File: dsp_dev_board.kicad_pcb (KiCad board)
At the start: 4 copper layers, 100 x 100 mm, 85 parts, among them J1 aux_mcu_power, J10 DX07S016JA1R1500, J2 audio_in, J3 audio_out, J4 9v_jack, J5 input_jack, J6 output_jack, J7 digital, J8 analog, J9 debug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

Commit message: WIP: QFN all the things
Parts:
- added J11: Conn_02x11_Odd_Even, Connector_PinHeader_2.54mm:PinHeader_2x11_P2.54mm_Vertical, F.Cu at (211.1, 104.0)
- added R11: 10k, Resistor_SMD:R_0603_1608Metric, F.Cu at (232.3, 109.6)
- added R23: 0 DNP, Resistor_SMD:R_0603_1608Metric, F.Cu at (210.8, 138.4)
- added R24: 0 DNP, Resistor_SMD:R_0603_1608Metric, F.Cu at (210.8, 140.9)
- added R25: 0 DNP, Resistor_SMD:R_0603_1608Metric, F.Cu at (214.8, 138.4)
- added R26: 0 DNP, Resistor_SMD:R_0603_1608Metric, F.Cu at (214.8, 140.9)
- added S1: TS-1187A-B-A-B, TactileSwitch:SW_TS-1187A-B-A-B, F.Cu at (235.3, 105.0)
- U3: value ATSAME51J18A-A -> ATSAME51J20A-A
- U4: value WM8731SEDS -> WM8731CLSEFL; footprint Package_SO:SSOP-28_5.3x10.2mm_P0.65mm -> Package_DFN_QFN:QFN-28-1EP_5x5mm_P0.5mm_EP3.35x3.35mm
- moved U4 1.96 mm to (156.2, 85.8), turned to 0 degrees
- moved R19 0.48 mm to (156.2, 79.7)
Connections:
- U4 pad 1: 3.3V -> /MCU/I2S2_MCK
- U4 pad 10: Net-(U4-Pad10) -> /Codec/ADC
- U4 pad 11: GND -> /Codec/WCLK
- U4 pad 12: /Codec/audio_out -> 3.3V
- U4 pad 14: 3.3V -> Net-(U4-Pad14)
- U4 pad 16: Net-(U4-Pad16) -> /Codec/audio_out
- U4 pad 18: Net-(U4-Pad18) -> 3.3V
- U4 pad 19: Net-(U4-Pad19) -> GND
- U4 pad 20: /Codec/audio_in -> Net-(U4-Pad20)
- U4 pad 21: Net-(R19-Pad1) -> Net-(U4-Pad21)
- U4 pad 22: /Codec/~CSB -> Net-(U4-Pad22)
- U4 pad 23: /Codec/SDIN -> Net-(U4-Pad23)
- U4 pad 24: /Codec/SCLK -> /Codec/audio_in
- U4 pad 25: /MCU/I2S2_MCK -> Net-(R19-Pad1)
- U4 pad 26: Net-(U4-Pad26) -> /Codec/~CSB
- U4 pad 27: 3.3V -> /Codec/SDIN
- U4 pad 28: GND -> /Codec/SCLK
- U4 pad 3: /Codec/BCLK -> 3.3V
- U4 pad 4: /Codec/DAC -> GND
- U4 pad 5: /Codec/WCLK -> 3.3V
- U4 pad 6: /Codec/ADC -> Net-(U4-Pad6)
- U4 pad 7: /Codec/WCLK -> /Codec/BCLK
- U4 pad 8: 3.3V -> /Codec/DAC
- U4 pad 9: Net-(U4-Pad9) -> /Codec/WCLK
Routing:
- net /Codec/SCLK: track 32.4 -> 0.00 mm, vias 2 -> 0
- net /Codec/SDIN: track 27.1 -> 0.00 mm, vias 2 -> 0
- net /Codec/BCLK: track 41.6 -> 17.8 mm
- net /audio_in: track 30.5 -> 15.3 mm
- net /Codec/WCLK: track 44.2 -> 29.6 mm
- net /MCU/I2S2_MCK: track 44.4 -> 31.8 mm
- net /Codec/ADC: track 51.6 -> 39.2 mm
- net GND: track 90.0 -> 84.2 mm, vias 16 -> 15
- net 3.3V: track 39.0 -> 34.0 mm
- net Net-(R19-Pad1): track 3.68 -> 0.00 mm
- net /Codec/DAC: track 48.9 -> 47.1 mm
- net /audio_out: track 42.6 -> 41.0 mm
- net /Codec/~CSB: track 33.2 -> 32.5 mm

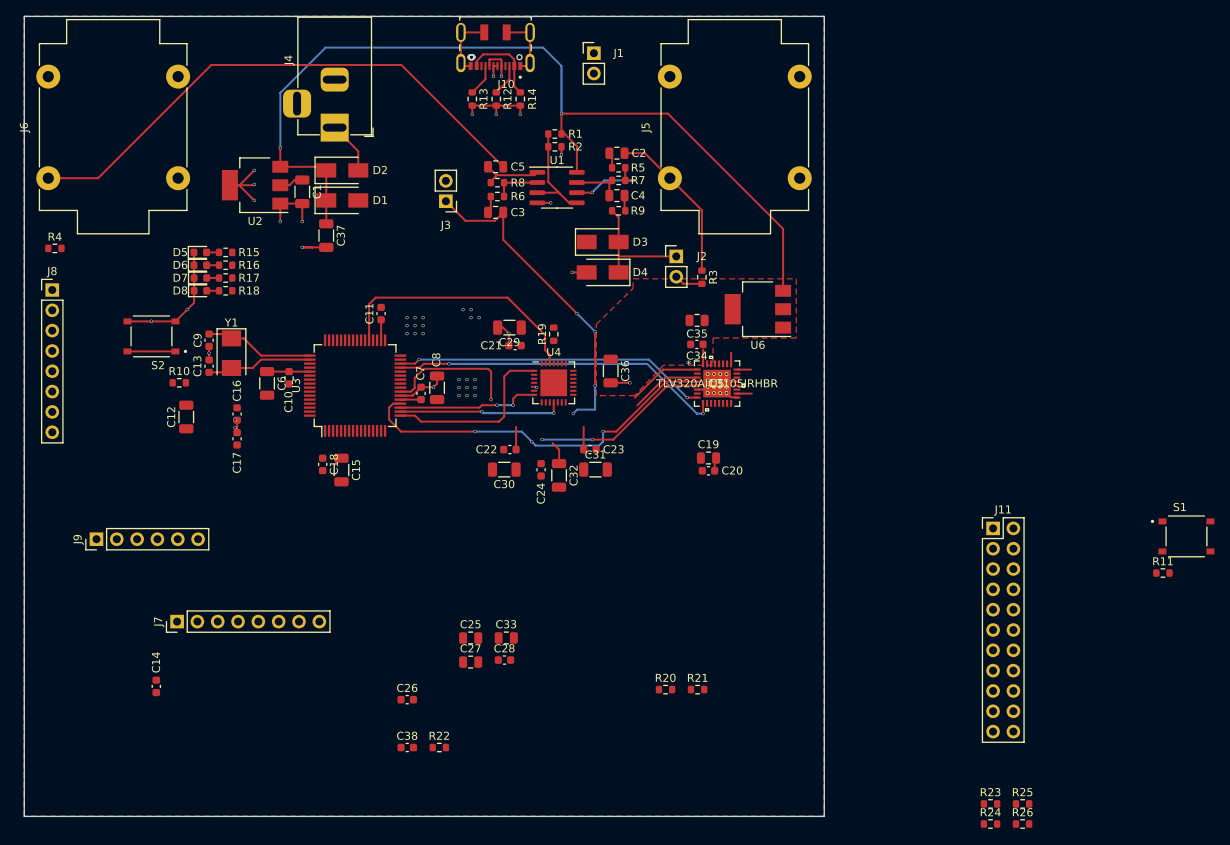
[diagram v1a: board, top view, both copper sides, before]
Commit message: pcb: everything connected, passes DRC
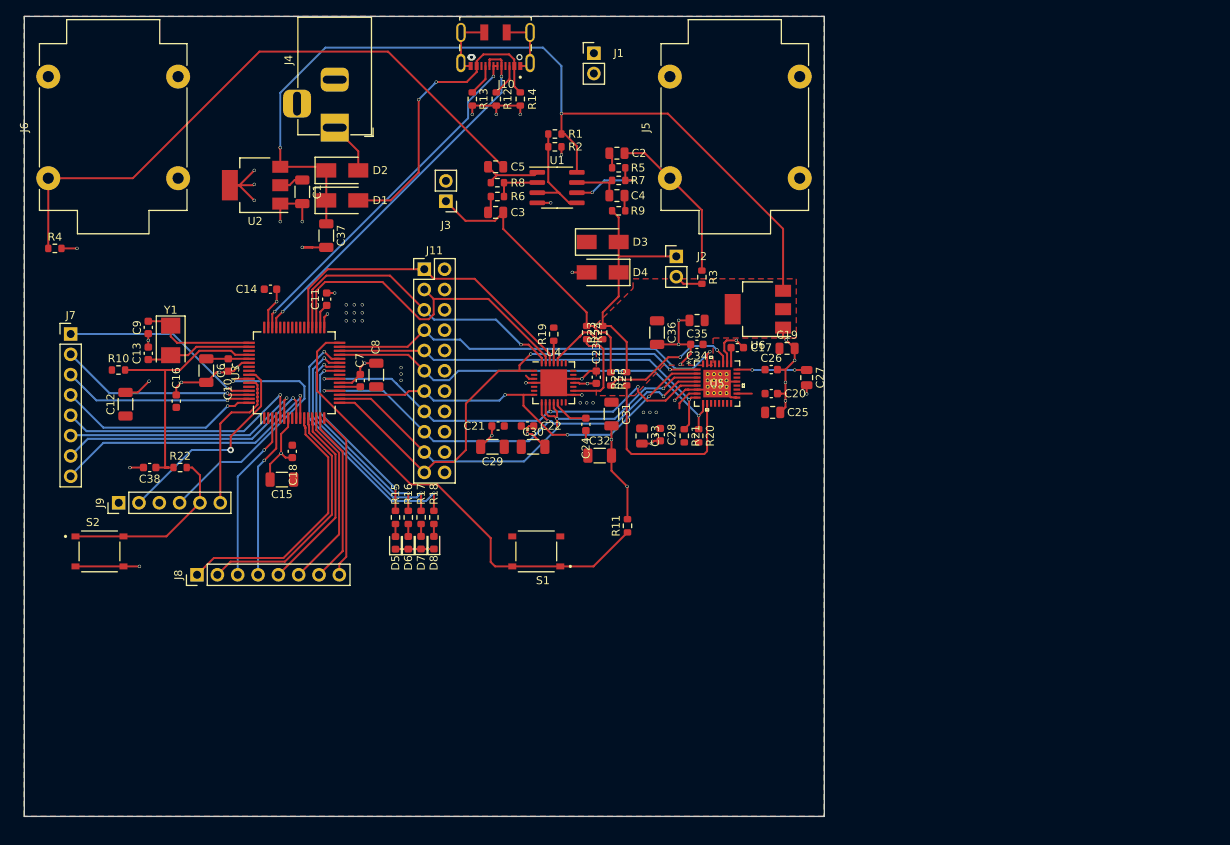
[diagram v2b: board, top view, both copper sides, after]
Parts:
- moved S1 81.3 mm to (154.0, 106.9), turned to 180 degrees
- moved R24 79.5 mm to (160.3, 79.5), turned to 270 degrees
- moved J11 78.1 mm to (140.0, 71.6)
- moved R23 76.3 mm to (162.3, 79.5), turned to 90 degrees
- moved R26 75.8 mm to (163.3, 85.3), turned to 270 degrees
- moved R25 72.6 mm to (165.3, 85.3), turned to 90 degrees
- moved R11 67.2 mm to (165.4, 103.7), turned to 90 degrees
- moved C17 63.6 mm to (179.1, 81.4), turned to 0 degrees
- moved C26 61.4 mm to (183.4, 84.2)
- moved C27 55.0 mm to (187.8, 85.2), turned to 270 degrees
- moved C14 51.7 mm to (120.8, 74.1), turned to 0 degrees
- moved R22 47.7 mm to (109.5, 96.4)
- moved C38 47.6 mm to (105.7, 96.4), turned to 180 degrees
- moved C25 47.1 mm to (183.6, 89.5)
- moved D5 43.7 mm to (136.4, 105.8), turned to 90 degrees
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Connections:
- J11 pad 11: /Codec/WCLK -> /MCU/SDA
- J11 pad 17: /MCU/SDA -> /Codec/DAC
- J11 pad 19: /MCU/SCL -> /Codec/WCLK
- J11 pad 21: /MCU/~CODEC_RST -> /MCU/I2S2_MCK
- J11 pad 7: /MCU/I2S2_MCK -> /MCU/~CODEC_RST
- J11 pad 9: /Codec/DAC -> /MCU/SCL
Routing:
- net GND: track 84.2 -> 184.2 mm, vias 15 -> 44
- net /MCU/BOOT0: track 0.00 -> 59.6 mm
- net /MCU/~CODEC_RST: track 0.00 -> 51.7 mm, vias 0 -> 1
- net /Codec/SDIN: track 0.00 -> 43.5 mm
- net /MCU/OTG_FS_DM: track 4.39 -> 47.4 mm, vias 1 -> 2
- net /MCU/OTG_FS_DP: track 1.82 -> 44.7 mm, vias 1 -> 2
- net /Codec/SCLK: track 0.00 -> 39.1 mm, vias 0 -> 1
- net /MCU/PB07: track 0.00 -> 35.9 mm, vias 0 -> 1
- net /Codec/BCLK: track 17.8 -> 53.1 mm, vias 2 -> 3
- net /MCU/led4: track 0.00 -> 33.9 mm, vias 0 -> 2
- net /MCU/SWDIO: track 0.00 -> 33.9 mm, vias 0 -> 1
- net /MCU/PB06: track 0.00 -> 33.5 mm, vias 0 -> 1
- net /MCU/PB08: track 0.00 -> 32.7 mm
- net Net-(C38-Pad1): track 0.00 -> 31.9 mm
- net /MCU/PB04: track 0.00 -> 31.8 mm, vias 0 -> 1
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
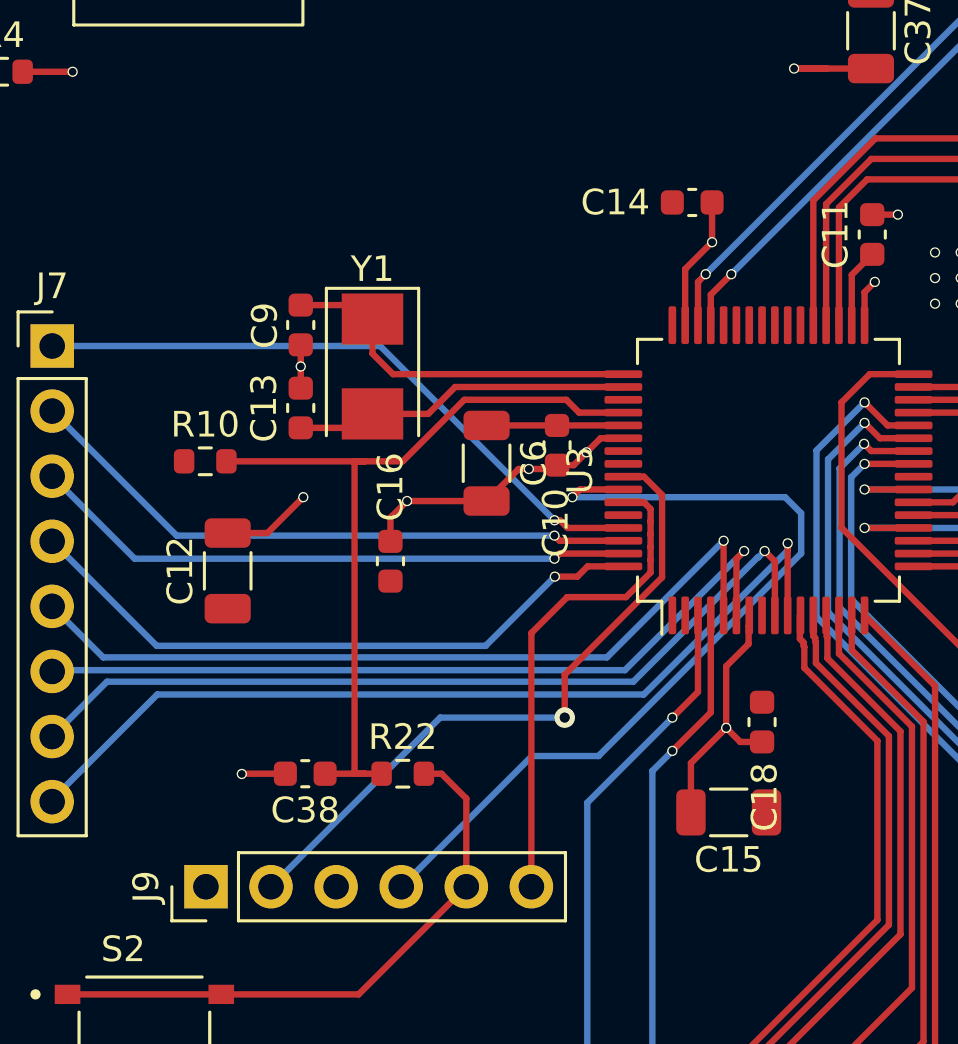
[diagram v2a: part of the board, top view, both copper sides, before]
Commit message: pcb: enhance bypassing on the left side of MCU
I stuck the bulk bypassing for VDDIO near pin 56, so nudge those
capacitors over so the F.Cu layer can connect them, and stitch that
through with some vias to the B.Cu +3.3V rail.
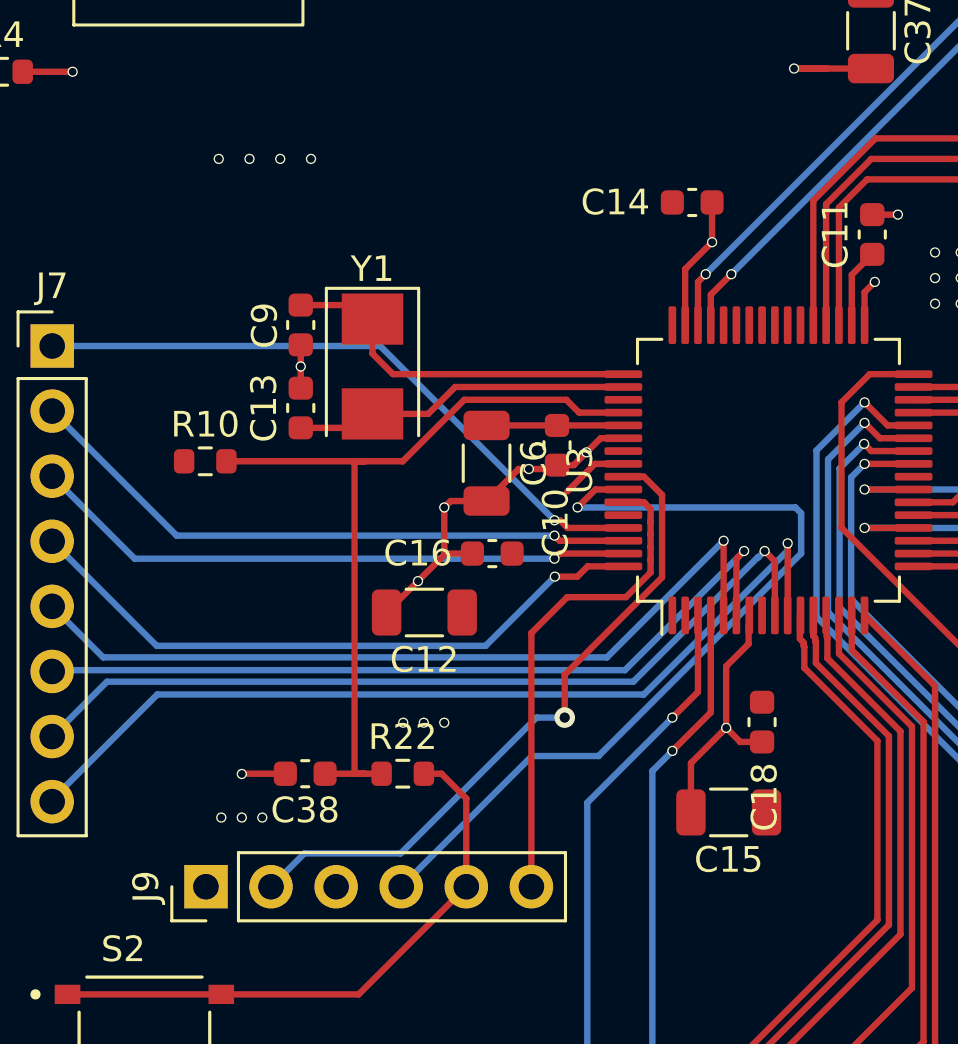
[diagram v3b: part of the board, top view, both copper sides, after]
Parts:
- moved C12 7.85 mm to (110.3, 90.1), turned to 180 degrees
- moved C16 3.99 mm to (113.0, 87.8), turned to 180 degrees
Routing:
- net 3.3V: track 43.9 -> 46.6 mm, vias 24 -> 34
- net GND: track 184.2 -> 183.7 mm

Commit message: pcb: nudge stuff around so it looks good
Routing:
- net 3.3V: vias 34 -> 36

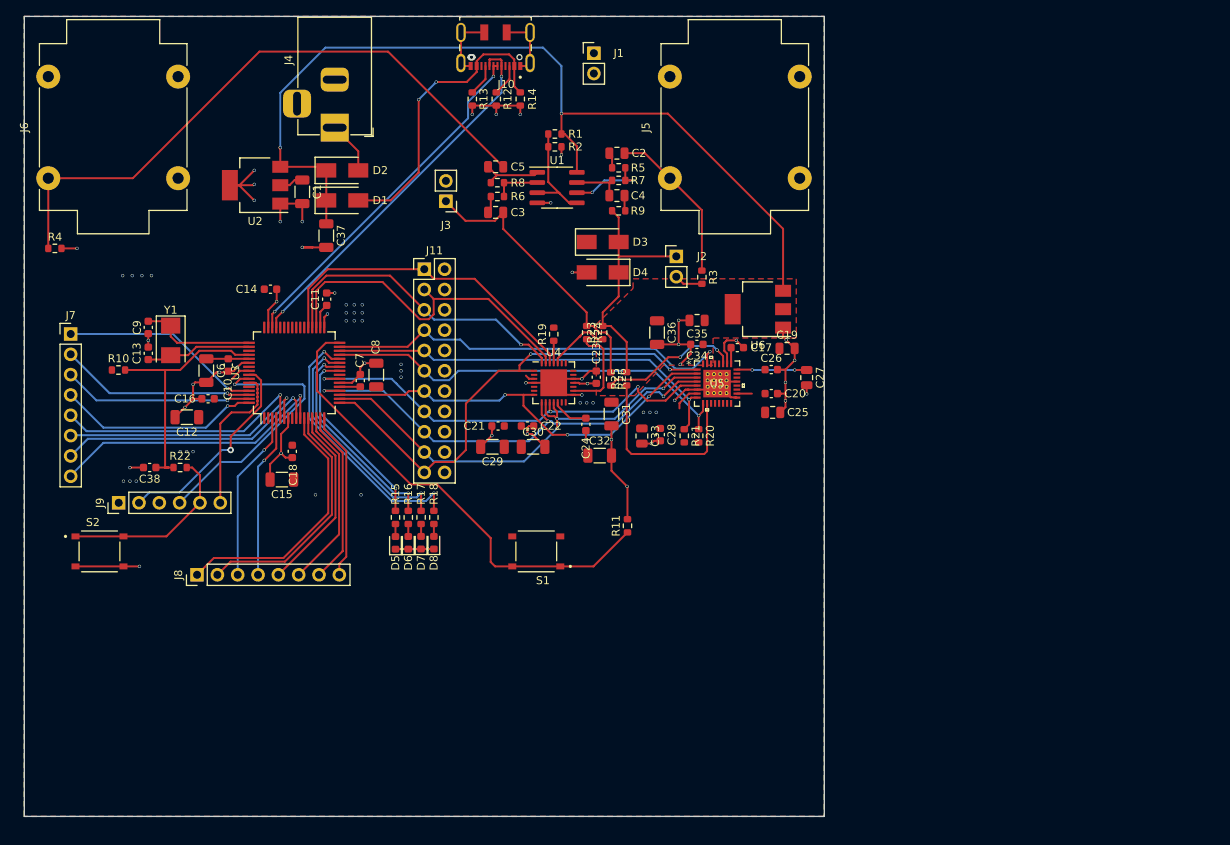
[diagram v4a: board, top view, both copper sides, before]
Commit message: pcb: move silkscreens so they're visible
Component references should not be over vias or other parts.  Move them
so they're visible, but maintain orientation -- the label is vertical if
the component is vertical.
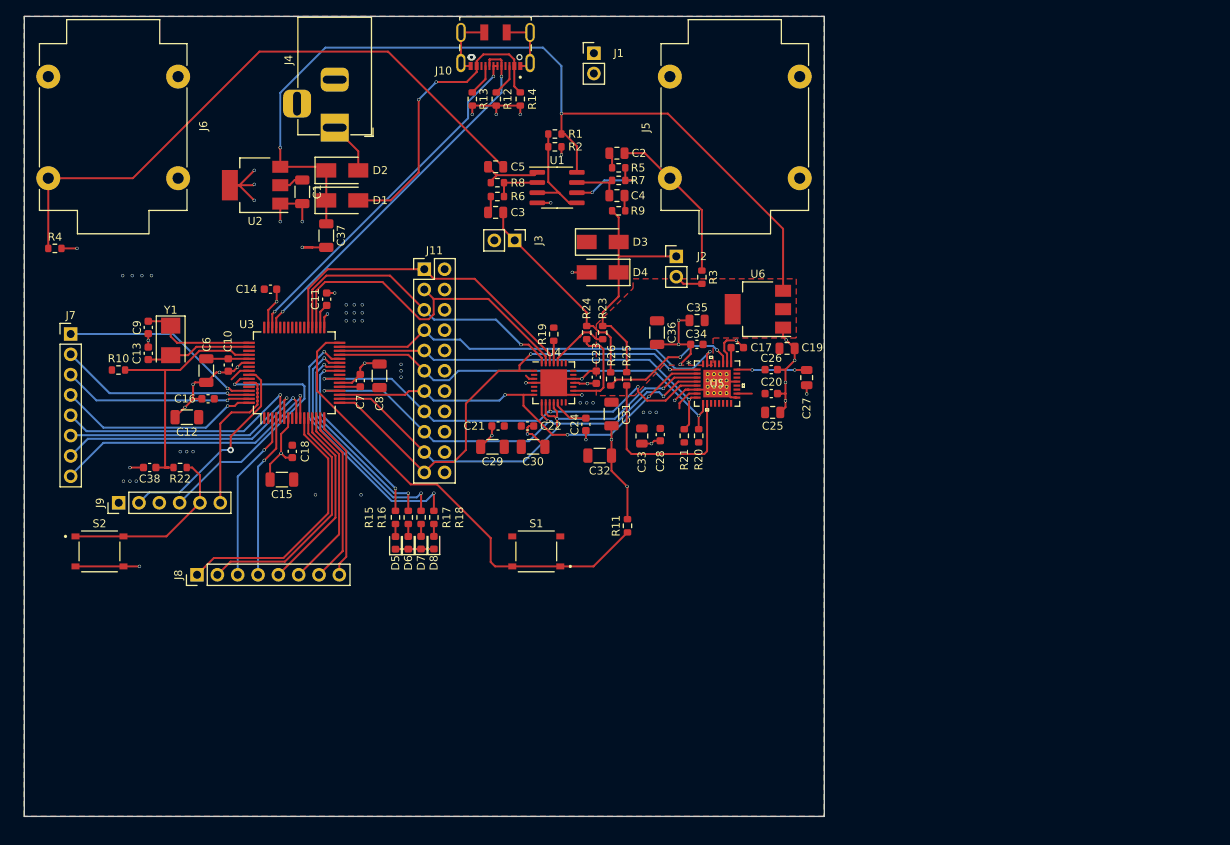
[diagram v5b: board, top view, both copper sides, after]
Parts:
- moved J3 9.90 mm to (151.3, 68.0), turned to 270 degrees
- moved C8 0.41 mm to (134.4, 84.9)
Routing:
- net /audio_out: track 35.1 -> 26.5 mm
